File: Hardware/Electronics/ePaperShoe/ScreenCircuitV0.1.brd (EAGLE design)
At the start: 22.8 x 36.5 mm, 15 parts, among them Q1 IRF7509, U1 XF2J-2624-11A, X1 FH12-26S-0.5SH

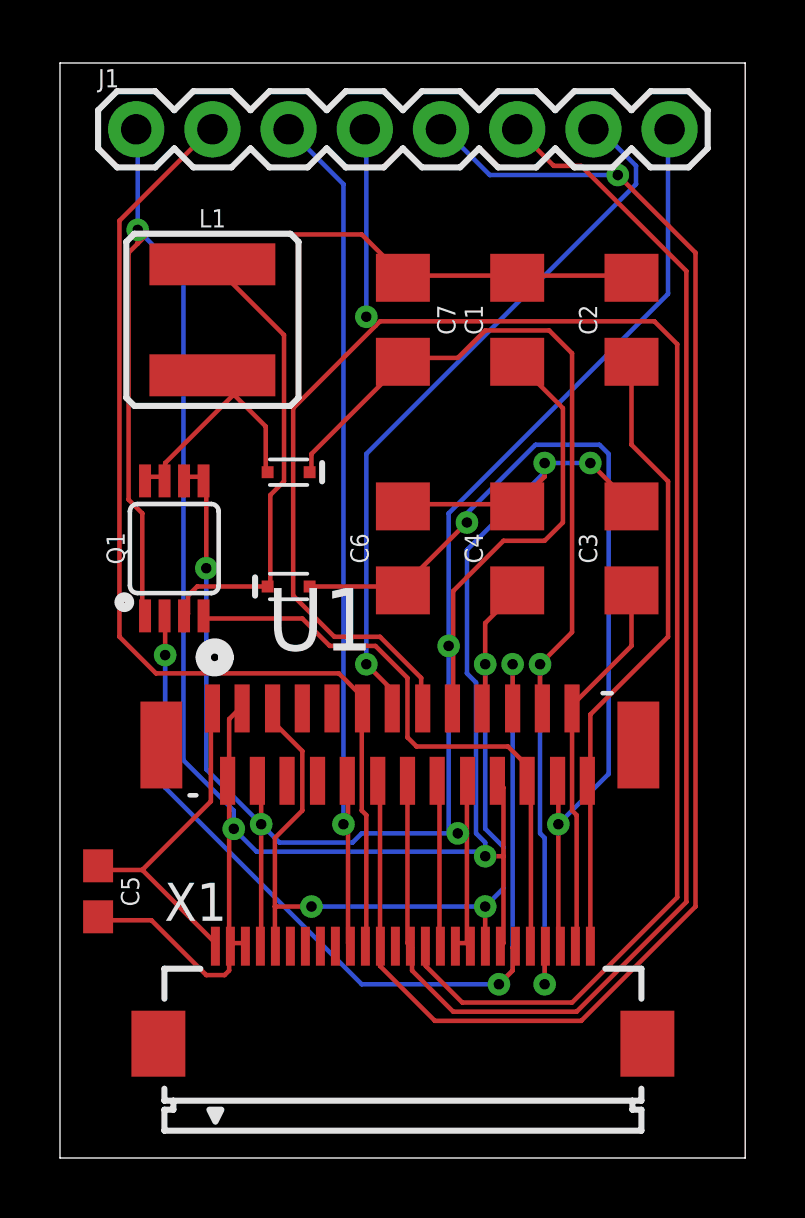
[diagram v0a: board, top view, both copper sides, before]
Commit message: Changes made to the screen circuit
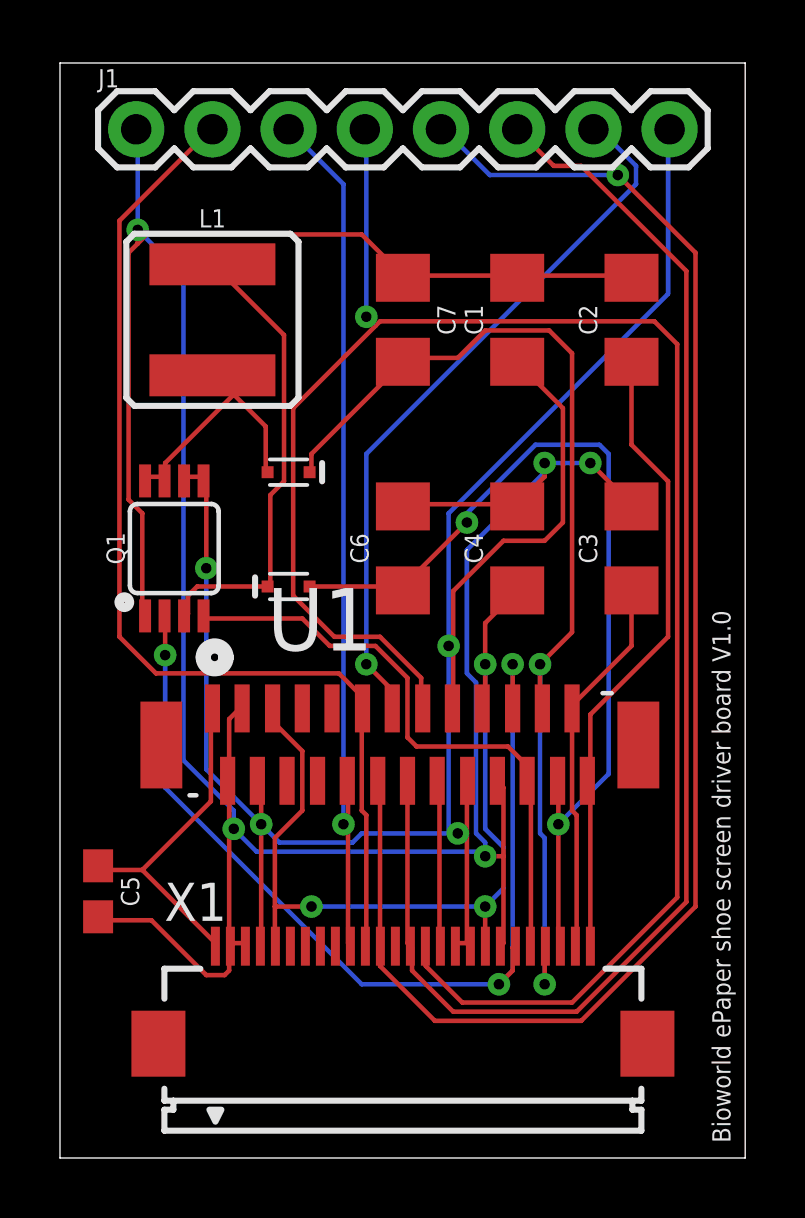
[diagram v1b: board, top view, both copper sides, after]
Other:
- board text added: "Bioworld ePaper shoe screen driver board V1.0"
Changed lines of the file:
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@@
 <?xml version="1.0" encoding="utf-8"?>
 <!DOCTYPE eagle SYSTEM "eagle.dtd">
-<eagle version="8.4.1">
+<eagle version="8.4.2">
 <drawing>
 <settings>
@@
 <wire x1="22.84" y1="36.5" x2="0" y2="36.5" width="0" layer="20"/>
 <wire x1="0" y1="36.5" x2="0" y2="0" width="0" layer="20"/>
+<text x="22.352" y="0.508" size="0.6096" layer="21" rot="R90">Bioworld ePaper shoe screen driver board V1.0</text>
 </plain>
 <attributes>
